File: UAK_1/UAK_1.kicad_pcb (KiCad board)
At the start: 2 copper layers, 100 x 90 mm, 80 parts, among them K1 Кнопка_FSMSM, K2 Кнопка_FSMSM, X1 Крепежное_отверстие_М3, X2 Крепежное_отверстие_М3, X3 Крепежное_отверстие_М3, X4 Крепежное_отверстие_М3, X5 Крепежное_отверстие_d2, X6 Крепежное_отверстие_d2, X7 Крепежное_отверстие_d2

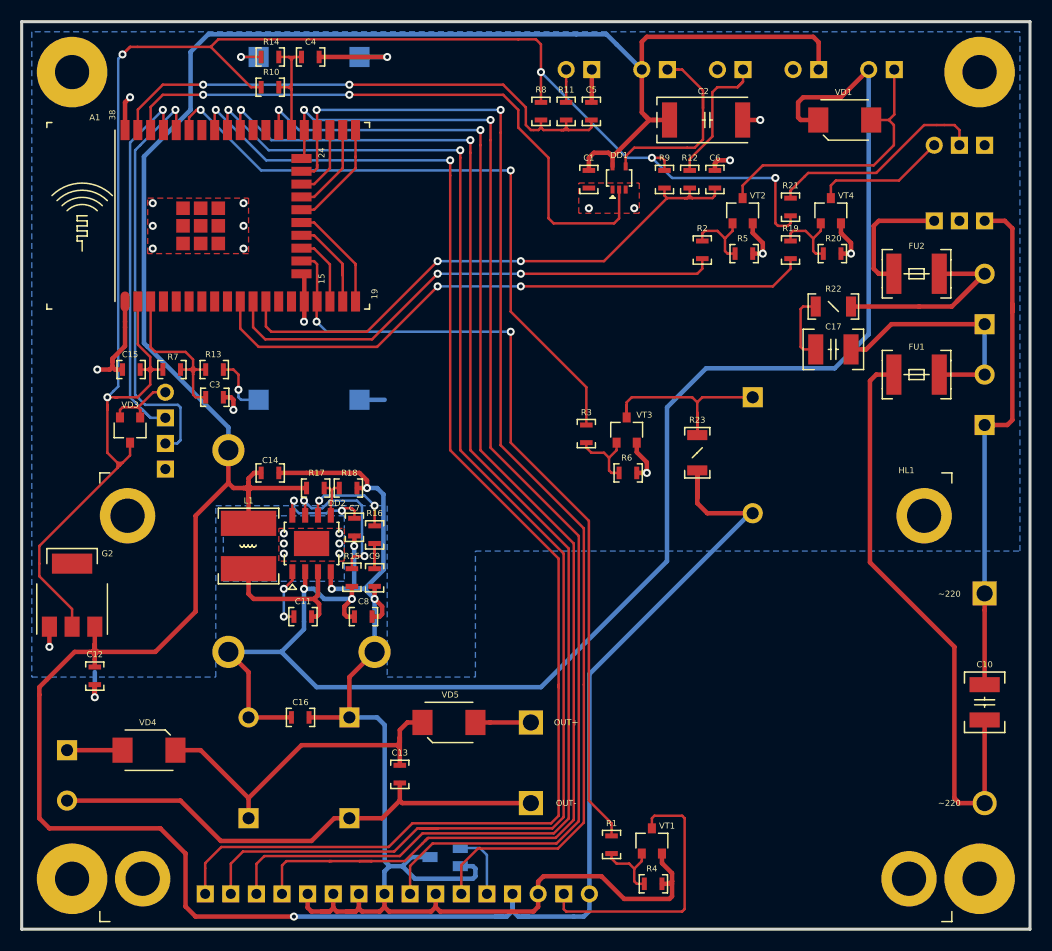
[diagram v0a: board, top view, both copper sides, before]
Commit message: 1B: заменены предохранители,обновлено питание,не добавлен второй дисплей
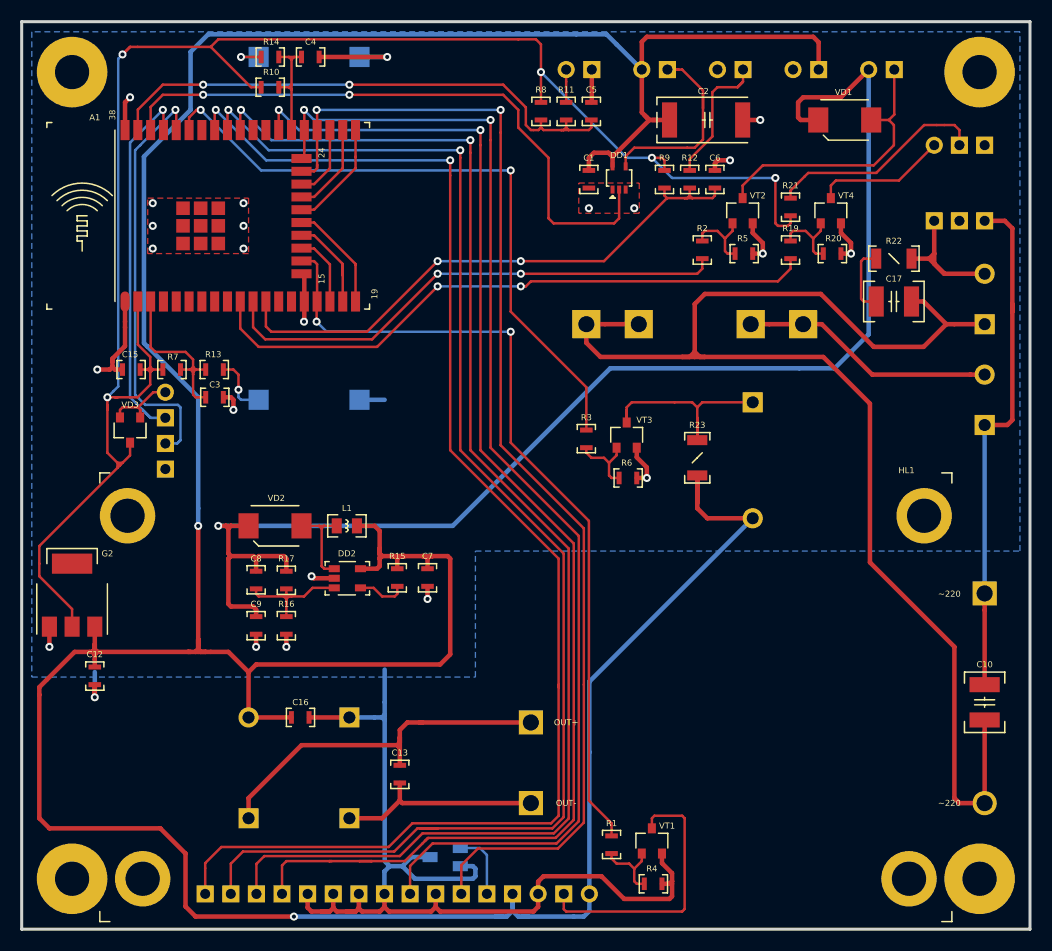
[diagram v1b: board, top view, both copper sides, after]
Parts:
- removed C11, C14: Конденсатор_керамический, N_RLC:Конденсатор_SMD_0603
- removed FU1, FU2: Предохранитель, N_RLC:Предохранитель_SMD_1812
- removed R18: Резистор_0,065Вт, N_RLC:Резистор_SMD_0603_0,065_Вт
- removed VD4, VD5: Диод_шоттки_SK16, N_VD_HL:Диод_SMB
- removed X5, X6, X7: Крепежное_отверстие_d2, MOTOR_ICO:Монтажное_отверстие_D2
- removed XT5: Клеммник_х2_KLS2-300-5.00-02P-2S, N_X:Клеммник_х2_шаг5
- added VD2: Диод_шоттки_SK16, N_VD_HL:Диод_SMB, F.Cu at (102.5, 100.0)
- added XFU1: Держатель_предохранителя_KLS5-266, N_X:Держатель_5х20, B.Cu at (131.0, 80.0)
- added XFU2: Держатель_предохранителя_KLS5-266, N_X:Держатель_5х20, B.Cu at (152.5, 80.0)
- DD2: value Микросхема_DCDC_step_DOWN_MP2307DN -> Микросхема_DCDC_step_UP_LM2703; footprint N_DD:SO-8_EP -> N_G:Преобразователь_LM2703_SOT-23-5
- G1: value AC-DC-преобразователь_IRM-20-12 -> AC-DC-преобразователь_IRM-15-5
- L1: value Чип-индуктивность_10мкГн_1.8А_20проц. -> Чип-индуктивность_10мкГн_0.2А_20проц.; footprint N_RLC:Чип-индуктивность_SMD_SCD0503T -> N_RLC:Чип-индуктивность_SMD_0805
- moved C9 12.7 mm to (98.2, 109.0)
- moved R16 12.6 mm to (101.2, 109.0)
- moved C8 10.1 mm to (98.2, 106.2), turned to 90 degrees
- moved C7 8.81 mm to (115.2, 104.2)
- moved L1 8.75 mm to (106.2, 100.0), turned to 0 degrees
- moved R17 8.49 mm to (101.2, 104.5), turned to 270 degrees
- moved C17 7.65 mm to (159.8, 77.8)
- moved R22 7.65 mm to (163.2, 73.5)
- moved R15 4.83 mm to (112.2, 104.2), turned to 270 degrees
- moved DD2 3.36 mm to (106.0, 104.2), turned to 270 degrees
- moved HA1 0.50 mm to (147.5, 93.5)
- moved R23 0.50 mm to (142.0, 95.0)
- moved R3 0.50 mm to (131.0, 92.2)
- moved R6 0.50 mm to (134.2, 95.2)
- moved VT3 0.50 mm to (135.0, 91.0)
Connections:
- net /0V_RES renamed Net-(C13-Pad2)
- C10 pad 1: /SUPPLY_POWER/220_L_FU -> /220_L_FU
- C13 pad 1: /SUPPLY_POWER/12V_NOISE -> /SUPPLY_POWER/5V_NOISE
- C16 pad 1: /12V -> /5V
- C17 pad 2: /220_L -> /220_L_FU
- C7 pad 1: Net-(C7-Pad1) -> /5V
- C8 pad 1: /12V -> Net-(C8-Pad1)
- C8 pad 2: /GND -> /12V
- C9 pad 1: Net-(C9-Pad1) -> /12V
- DA1 pad 6: /220_N_FU -> /220_N_OUT
- DD2 pad 1: Net-(C11-Pad1) -> Net-(DD2-Pad1)
- DD2 pad 2: /12V -> /GND
- DD2 pad 3: /SUPPLY_POWER/5V_DC-DC -> Net-(C8-Pad1)
- DD2 pad 4: /GND -> Net-(DD2-Pad4)
- DD2 pad 5: Net-(DD2-Pad5) -> /5V
- G1 pad +V: /SUPPLY_POWER/12V_OUT_G -> /SUPPLY_POWER/5V_NOISE
- G1 pad L: /SUPPLY_POWER/220_L_FU -> /220_L_FU
- L1 pad 1: /5V -> Net-(DD2-Pad1)
- L1 pad 2: /SUPPLY_POWER/5V_DC-DC -> /5V
- L2 pad 1: /12V -> /5V
- L2 pad 6: /SUPPLY_POWER/12V_NOISE -> /SUPPLY_POWER/5V_NOISE
- R15 pad 1: /12V -> /5V
- R15 pad 2: Net-(DD2-Pad7) -> Net-(DD2-Pad4)
- R16 pad 1: Net-(DD2-Pad6) -> Net-(C8-Pad1)
- R16 pad 2: Net-(C9-Pad1) -> /GND
- R17 pad 1: /5V -> /12V
- R17 pad 2: Net-(DD2-Pad5) -> Net-(C8-Pad1)
- XT8 pad 2: /220_L -> /220_L_FU
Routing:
- net /220_L_FU: track 0.00 -> 136.3 mm
- net /SUPPLY_POWER/220_L_FU: track 58.9 -> 0.00 mm
- net /5V: track 330.3 -> 381.9 mm, vias 1 -> 2
- net /GND: track 207.2 -> 166.7 mm
- net /SUPPLY_POWER/5V_NOISE: track 0.00 -> 37.2 mm
- net /SUPPLY_POWER/12V_NOISE: track 35.4 -> 0.00 mm
- net Net-(C13-Pad2): track 51.2 -> 20.6 mm
- net /12V: track 156.4 -> 134.0 mm, vias 2 -> 1
- net Net-(DD2-Pad7): track 15.5 -> 0.00 mm, vias 2 -> 0
- net /SUPPLY_POWER/5V_DC-DC: track 14.6 -> 0.00 mm
- net Net-(C8-Pad1): track 0.00 -> 12.9 mm
- net /220_N_FU: track 12.7 -> 0.00 mm
- net Net-(DD2-Pad6): track 9.62 -> 0.00 mm, vias 2 -> 0
- net Net-(C7-Pad1): track 9.54 -> 0.00 mm, vias 2 -> 0
- net Net-(DD2-Pad1): track 0.00 -> 9.31 mm
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- removed copper zone on B.Cu, net BOTTOM
- removed copper zone on F.Cu, net BOTTOM
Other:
- board text added: "UAK.1B.M9"
- board text removed: "12V"
- board text removed: "5V"
- board text removed: "EXT_0V IN"
- board text removed: "EXT_12V IN"
- board text removed: "UAK.1A.M9"

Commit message: обновлен перечень элементов
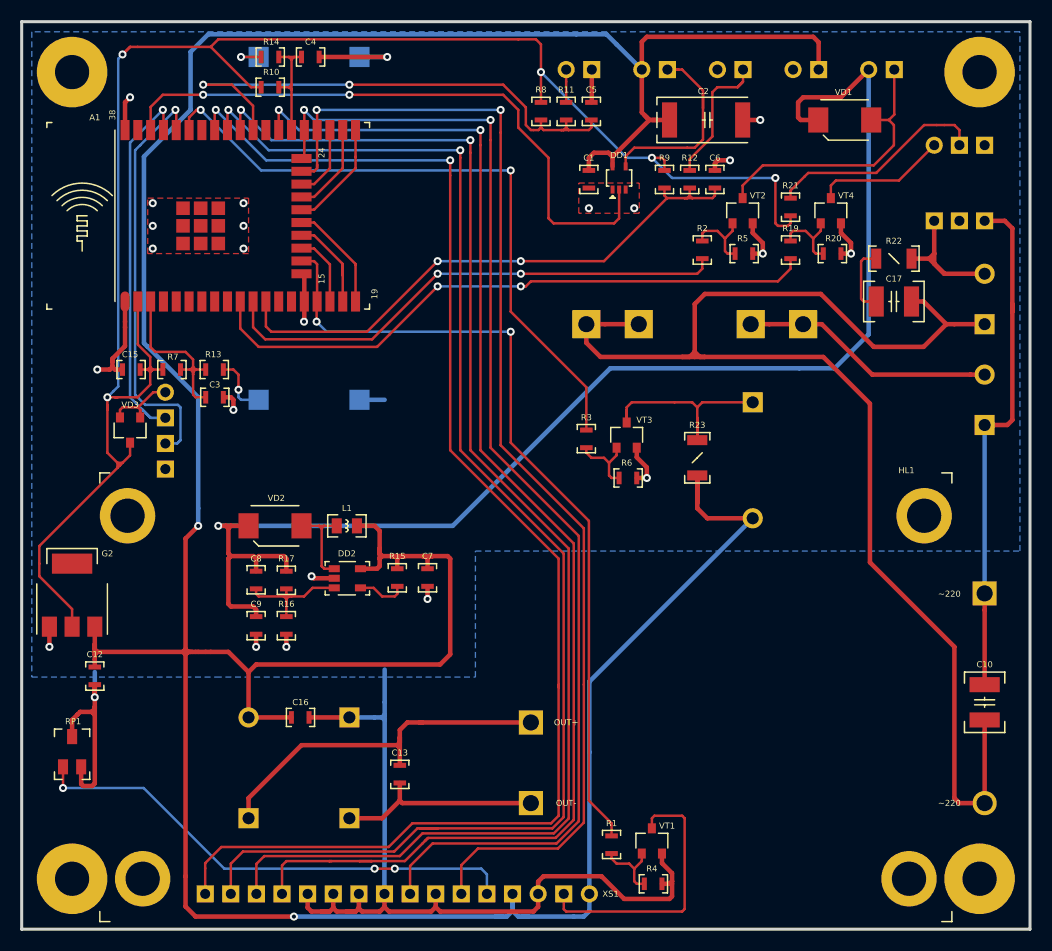
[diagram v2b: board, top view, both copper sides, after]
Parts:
- added D2: LOGO, N_ICO:danger_220, B.Cu at (141.7, 72.2)
- RP1: moved to F.Cu
- moved RP1 38.4 mm to (80.0, 122.4), turned to 0 degrees
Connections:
- A1 pad 28: Net-(A1-Pad28) -> /DOOR_SENSOR
- A1 pad 37: /DOOR_SENSOR -> /MOSI
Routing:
- net Net-(HL1-Pad3): track 6.79 -> 49.6 mm, vias 0 -> 3
- net /5V: track 381.9 -> 364.3 mm
- net /GND: track 166.7 -> 168.8 mm
- net /DOOR_SENSOR: track 54.4 -> 53.1 mm
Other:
- board text added: "5V_OUT"
- board text added: "XS1"

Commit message: UAK.1C.M9, подготовлены gerber, схема, BOM
обновлена маркировка, заполнен BOM
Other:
- board text added: "UAK.1С.M9"
- board text removed: "UAK.1B.M9"
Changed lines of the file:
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@@
-(kicad_pcb (version 20171130) (host pcbnew "(5.1.4)-1")
+(kicad_pcb (version 20171130) (host pcbnew "(5.1.2-1)-1")
   (general
     (thickness 1.6)
@@
     (effects (font (size 0.8 0.8) (thickness 0.15)) (justify mirror))
   )
-  (gr_text UAK.1B.M9 (at 145 137.5) (layer B.SilkS)
+  (gr_text UAK.1С.M9 (at 145 137.5) (layer B.SilkS)
     (effects (font (size 1 1) (thickness 0.15)) (justify mirror))
   )

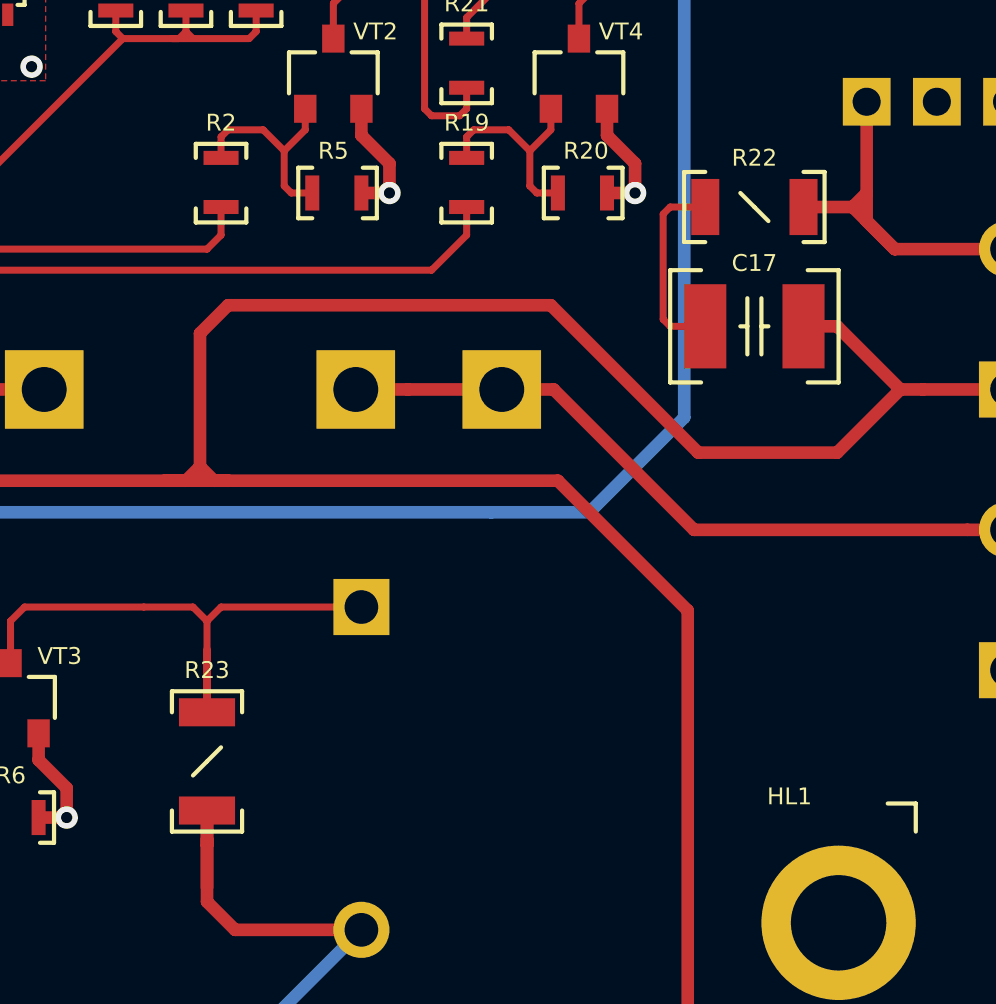
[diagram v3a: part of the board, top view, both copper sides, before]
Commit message: обновлены 3D в проекте и step
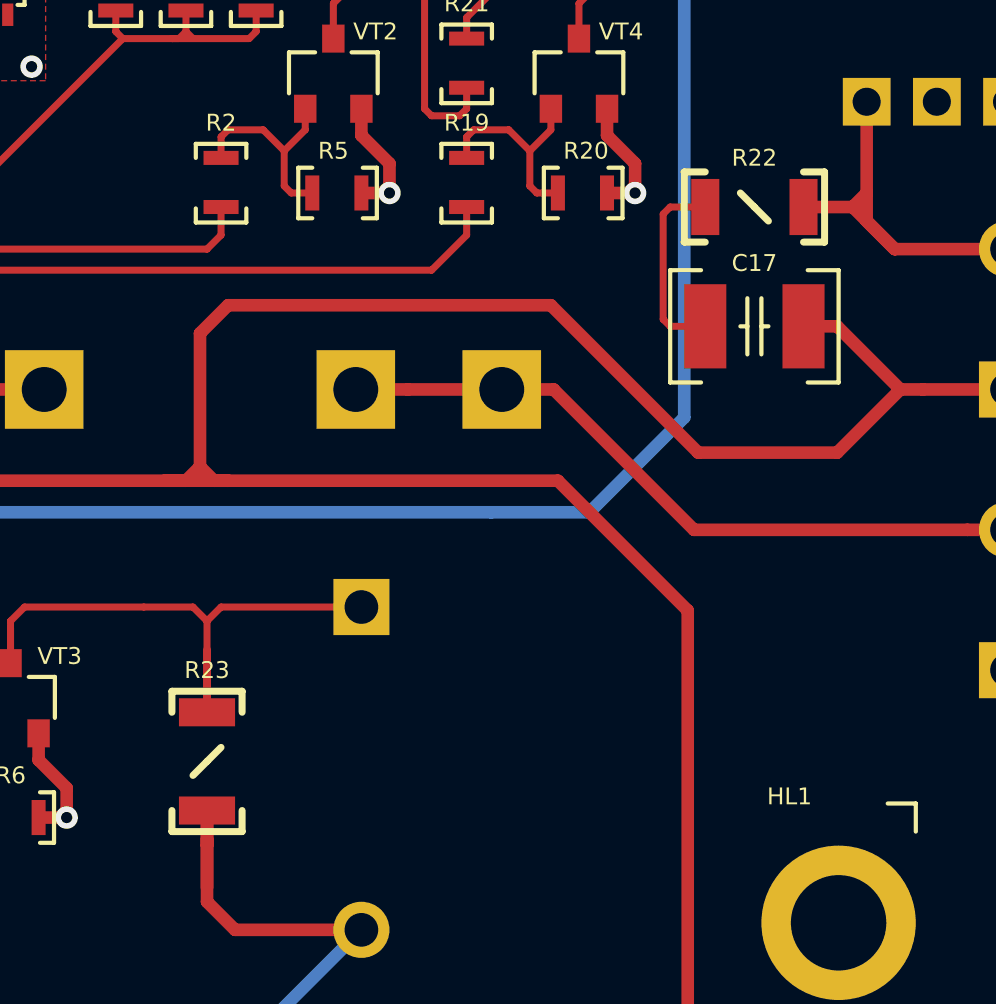
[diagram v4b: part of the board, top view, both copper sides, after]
